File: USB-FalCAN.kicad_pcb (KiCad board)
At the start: 4 copper layers, 76.5 x 30.9 mm, 59 parts, among them J1 Conn_01x17_Pin, J10 CAN, J2 NC, J3 Conn_01x17_Pin, J4 USB2.0_16P, J5 Boot, J6 NC, J7 DE9_Receptacle, J8 RS-485/422-TX, J9 RS-422-RX, SW3 BTN, U1 STM32F042C6Tx, U2 SN65HVD230, U3 SP3485EN, U4 SP3485EN, U5 MIC5504-3.3YM5, Y1 8MHz, Y2 32768Hz

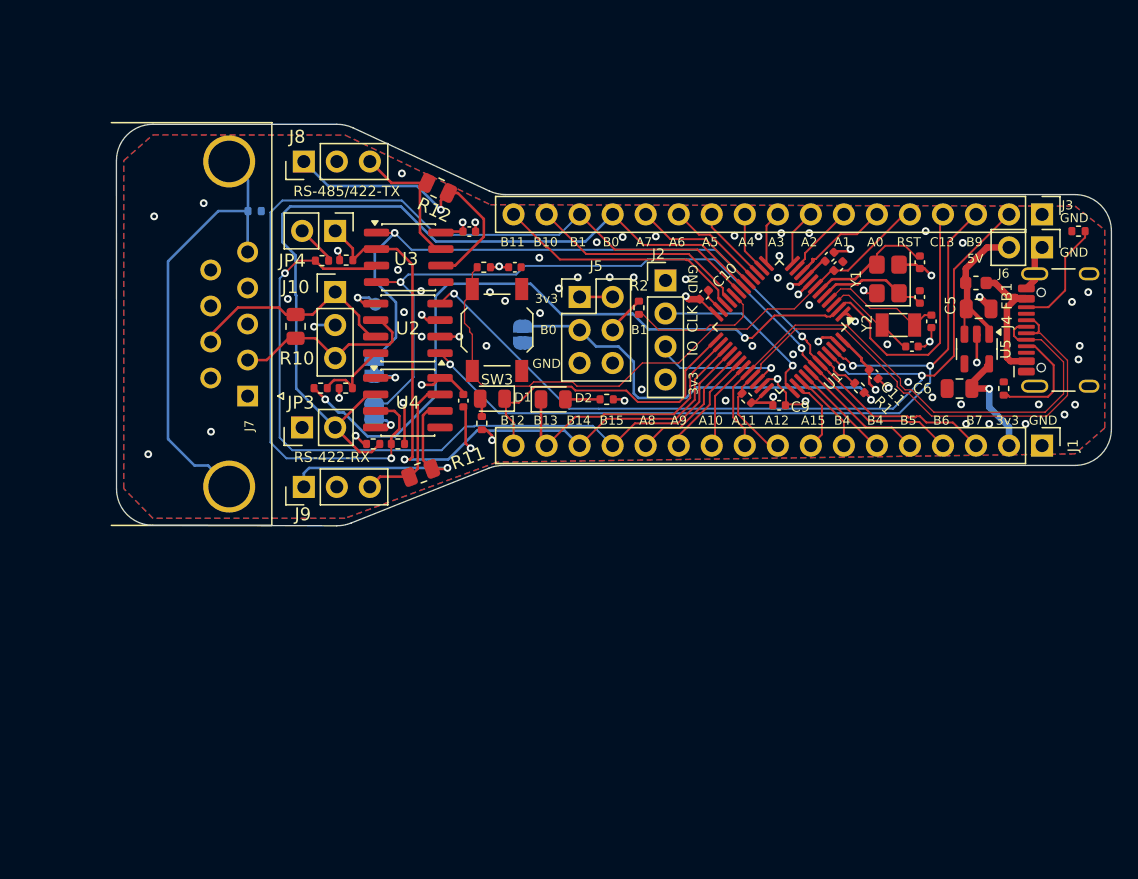
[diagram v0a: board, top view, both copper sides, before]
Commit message: feat: rerouting started
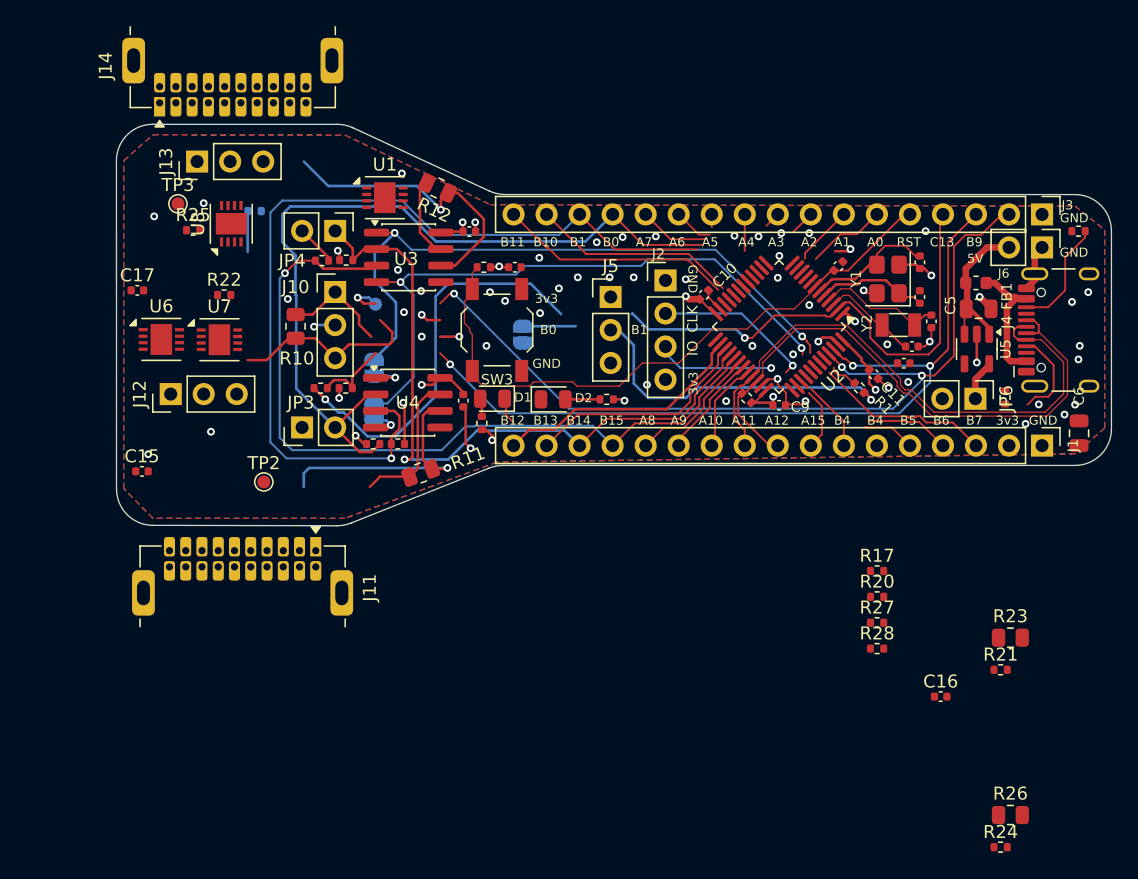
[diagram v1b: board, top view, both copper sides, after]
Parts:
- removed J7: DE9_Receptacle, Connector_Dsub:DSUB-9_Female_Horizontal_P2.77x2.84mm_EdgePinOffset7.70mm_Housed_MountingHolesOffset9.12mm
- removed J8: RS-485/422-TX, Connector_PinHeader_2.54mm:PinHeader_1x03_P2.54mm_Vertical
- removed J9: RS-422-RX, Connector_PinHeader_2.54mm:PinHeader_1x03_P2.54mm_Vertical
- removed R2: 10k, Resistor_SMD:R_0402_1005Metric
- added C15: 100nF, Capacitor_SMD:C_0402_1005Metric, F.Cu at (134.0, 84.5)
- added C16: 100nF, Capacitor_SMD:C_0402_1005Metric, F.Cu at (195.4, 101.8)
- added C17: 100nF, Capacitor_SMD:C_0402_1005Metric, F.Cu at (133.6, 70.6)
- added J11: G125-MH12005L1R, Harwin_Gecko:Harwin_G125-MH12005L1R_2x10_P1.25mm_Horizontal, F.Cu at (147.4, 90.6)
- added J12: CAN, Connector_PinHeader_2.54mm:PinHeader_1x03_P2.54mm_Vertical, F.Cu at (136.2, 78.6)
- added J13: CAN, Connector_PinHeader_2.54mm:PinHeader_1x03_P2.54mm_Vertical, F.Cu at (138.2, 60.7)
- added J14: G125-MH12005L1R, Harwin_Gecko:Harwin_G125-MH12005L1R_2x10_P1.25mm_Horizontal, F.Cu at (135.3, 56.2)
- added JP6: USE_LDO, Connector_PinHeader_2.54mm:PinHeader_1x02_P2.54mm_Vertical, F.Cu at (198.1, 78.9)
- added R17: 10, Resistor_SMD:R_0402_1005Metric, F.Cu at (190.5, 92.2)
- added R20: 10, Resistor_SMD:R_0402_1005Metric, F.Cu at (190.5, 94.2)
- added R21: 5k1, Resistor_SMD:R_0402_1005Metric, F.Cu at (200.0, 99.8)
- added R22: 100k, Resistor_SMD:R_0402_1005Metric, F.Cu at (140.3, 71.0)
- added R23: Rt, Resistor_SMD:R_0805_2012Metric, F.Cu at (200.8, 97.3)
- added R24: 5k1, Resistor_SMD:R_0402_1005Metric, F.Cu at (200.0, 113.4)
- added R25: 100k, Resistor_SMD:R_0402_1005Metric, F.Cu at (137.9, 66.0)
- added R26: Rt, Resistor_SMD:R_0805_2012Metric, F.Cu at (200.8, 111.0)
- added R27: 10, Resistor_SMD:R_0402_1005Metric, F.Cu at (190.5, 96.2)
- added R28: 10k, Resistor_SMD:R_0402_1005Metric, F.Cu at (190.5, 98.2)
- added TP2: VCC/2, TestPoint:TestPoint_Pad_D1.0mm, F.Cu at (143.4, 85.3)
- added TP3: VCC/2, TestPoint:TestPoint_Pad_D1.0mm, F.Cu at (136.8, 64.0)
- added U6: LTC2875-DD, Package_DFN_QFN:DFN-8-1EP_3x3mm_P0.5mm_EP1.66x2.38mm, F.Cu at (135.5, 74.4)
- added U7: LTC2875-DD, Package_DFN_QFN:DFN-8-1EP_3x3mm_P0.5mm_EP1.66x2.38mm, F.Cu at (139.9, 74.4)
- added U8: LTC2875-DD, Package_DFN_QFN:DFN-8-1EP_3x3mm_P0.5mm_EP1.66x2.38mm, F.Cu at (140.9, 65.5)
- C2, C3: value 15pF -> 10pF
- J5: footprint Connector_PinHeader_2.54mm:PinHeader_2x03_P2.54mm_Vertical -> Connector_PinHeader_2.54mm:PinHeader_1x03_P2.54mm_Vertical
- R18: value 100k -> 10k
- U1: value STM32F042C6Tx -> LTC4303IDD; footprint Package_QFP:LQFP-48_7x7mm_P0.5mm -> Package_DFN_QFN:DFN-8-1EP_3x3mm_P0.5mm_EP1.66x2.38mm
- U2: value SN65HVD230 -> STM32G474CETx; footprint Package_SO:SOIC-8_3.9x4.9mm_P1.27mm -> Package_QFP:LQFP-48_7x7mm_P0.5mm
- Y1: value 8MHz -> 16MHz AECQ200
- moved U1 31.9 mm to (152.7, 63.5), turned to 0 degrees
- moved U2 28.5 mm to (183.0, 73.4), turned to -135 degrees
- moved C8 9.98 mm to (192.6, 76.2), turned to 0 degrees
- moved C6 9.82 mm to (206.0, 81.6), turned to 90 degrees
- moved J5 2.39 mm to (170.0, 71.1)
- moved R13 0.69 mm to (200.4, 78.8)
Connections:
- net Net-(J8-Pin_1) renamed /485_TX_H
- net Net-(J8-Pin_3) renamed /485_TX_L
- net Net-(J9-Pin_1) renamed /485_RX_H
- net Net-(J9-Pin_3) renamed /485_RX_L
- C2 pad 1: Net-(U1-PF1) -> Net-(U2-PF1)
- C3 pad 1: Net-(U1-PF0) -> Net-(U2-PF0)
- C4 pad 1: Net-(U1-PC14) -> Net-(U2-PC14)
- C7 pad 1: Net-(U1-PC15) -> Net-(U2-PC15)
- D1 pad 1: /PB12 -> /PA5
- D2 pad 1: /PB13 -> /PA4
- J1 pad 16: /PB13 -> /CAN2_TX
- J1 pad 17: /PB12 -> /CAN2_RX
- J1 pad 6: /PB4 -> /CAN3_TX
- J1 pad 7: /PB3 -> /CAN3_RX
- J10 pad 1: /CAN_H -> /CAN1_H
- J10 pad 3: /CAN_L -> /CAN1_L
- J5 pad 2: +3V3 -> /BOOT0
- J5 pad 3: /BOOT0 -> GND
- R1 pad 2: Net-(U1-PF11) -> /CAN_RX
- R10 pad 1: /CAN_H -> /CAN1_H
- R10 pad 2: /CAN_L -> /CAN1_L
- R15 pad 2: Net-(U2-Rs) -> Net-(U6-RS)
- R16 pad 1: Net-(U2-Rs) -> Net-(U6-RS)
- R18 pad 2: Net-(J7-PAD) -> Net-(U1-RDY)
- TP1 pad 1: Net-(U2-Vref) -> Net-(U6-SPLIT)
- U1 pad 1: +3V3 -> Net-(U1-EN)
- U1 pad 2: /PC13 -> /SCL_OUT
- U1 pad 3: Net-(U1-PC14) -> /I2C1_SCL
- U1 pad 4: Net-(U1-PC15) -> GND
- U1 pad 5: Net-(U1-PF0) -> Net-(U1-RDY)
- U1 pad 6: Net-(U1-PF1) -> /I2C1_SDA
- U1 pad 7: /~{NRST} -> /SDA_OUT
- U1 pad 8: GND -> Net-(U1-VCC)
- U1 pad 9: +3V3 -> GND
- U2 pad 1: /CAN_TX -> +3V3
- U2 pad 2: GND -> /PC13
- U2 pad 3: +3V3 -> Net-(U2-PC14)
- U2 pad 4: /CAN_RX -> Net-(U2-PC15)
- U2 pad 5: Net-(U2-Vref) -> Net-(U2-PF0)
- U2 pad 6: /CAN_L -> Net-(U2-PF1)
- U2 pad 7: /CAN_H -> /~{NRST}
- U2 pad 8: Net-(U2-Rs) -> /PA0
- U5 pad 5: +3V3 -> Net-(JP6-A)
- Y1 pad 1: Net-(U1-PF0) -> Net-(U2-PF0)
- Y1 pad 3: Net-(U1-PF1) -> Net-(U2-PF1)
- Y2 pad 1: Net-(U1-PC15) -> Net-(U2-PC15)
- Y2 pad 2: Net-(U1-PC14) -> Net-(U2-PC14)
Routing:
- net Net-(J7-PAD): track 35.2 -> 0.00 mm
- net /PB12: track 23.1 -> 0.00 mm
- net /PB13: track 20.7 -> 0.00 mm
- net /CAN2_RX: track 0.00 -> 19.6 mm
- net /CAN2_TX: track 0.00 -> 17.6 mm
- net /CAN_H: track 16.0 -> 0.00 mm
- net /CAN_L: track 14.5 -> 0.00 mm
- net /CAN1_L: track 0.00 -> 14.5 mm
- net +3V3: track 42.3 -> 28.7 mm, vias 14 -> 12
- net /PB2: track 10.8 -> 0.00 mm
- net Net-(U2-PF1): track 0.00 -> 9.76 mm
- net Net-(U1-PF1): track 9.76 -> 0.00 mm
- net Net-(U2-PC15): track 0.00 -> 9.58 mm
- net Net-(U1-PC15): track 9.58 -> 0.00 mm
- net /CAN1_H: track 0.00 -> 8.34 mm
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
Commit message: feat: more routing
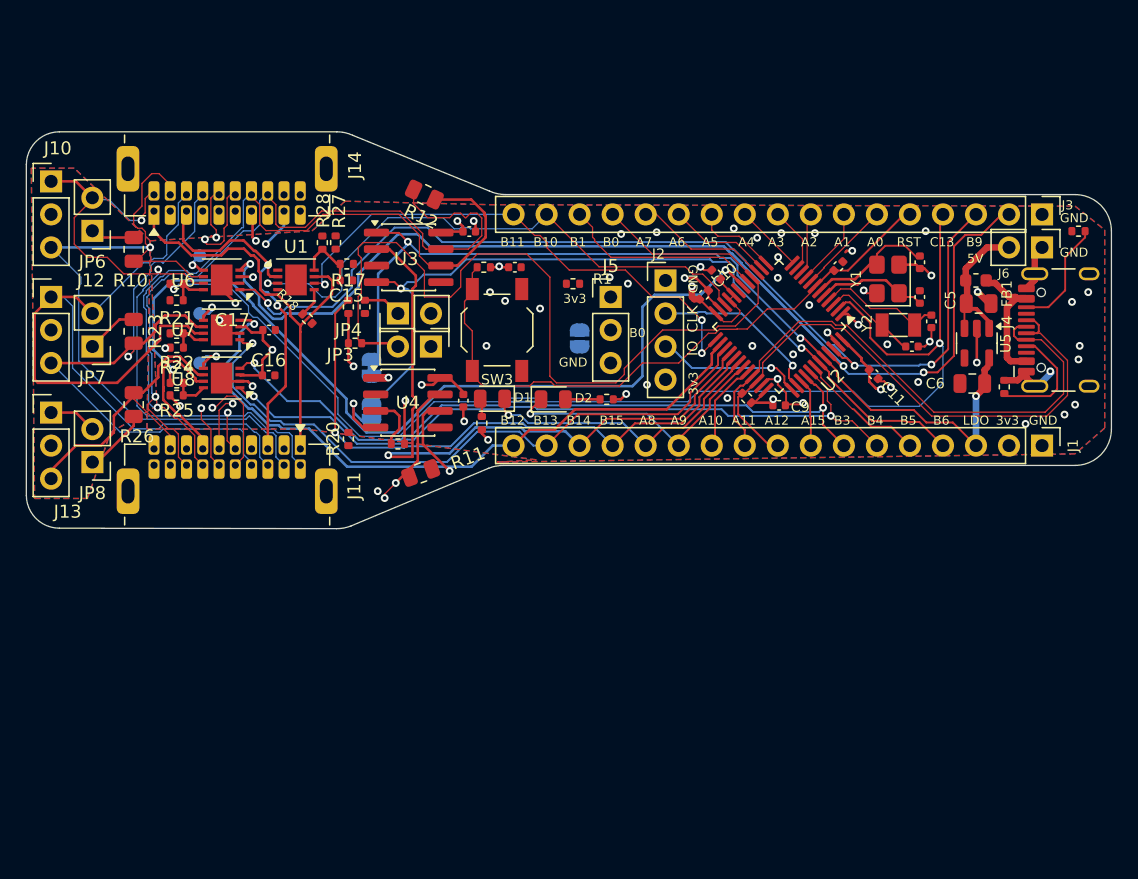
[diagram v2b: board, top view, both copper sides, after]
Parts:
- added JP7: Jumper_2_Open, Connector_PinHeader_2.54mm:PinHeader_1x02_P2.54mm_Vertical, F.Cu at (130.2, 74.9)
- added JP8: Jumper_2_Open, Connector_PinHeader_2.54mm:PinHeader_1x02_P2.54mm_Vertical, F.Cu at (130.2, 83.8)
- JP6: value USE_LDO -> Jumper_2_Open
- R18: moved to F.Cu
- TP2, TP3: moved to B.Cu
- moved R26 74.4 mm to (133.3, 79.4), turned to 90 degrees
- moved R24 72.7 mm to (136.7, 77.7)
- moved R23 71.4 mm to (133.3, 73.8), turned to -90 degrees
- moved JP6 69.1 mm to (130.2, 66.0), turned to 180 degrees
- moved R21 68.4 mm to (136.7, 73.9)
- moved C16 57.3 mm to (143.7, 77.1)
- moved R28 52.9 mm to (147.9, 66.9), turned to 90 degrees
- moved R27 50.9 mm to (148.9, 66.9), turned to -90 degrees
- moved R17 47.1 mm to (149.7, 68.6), turned to 180 degrees
- moved R20 42.4 mm to (149.9, 82.0), turned to 90 degrees
- moved J10 23.4 mm to (127.0, 62.2)
- moved R1 23.4 mm to (167.1, 70.1), turned to 180 degrees
- moved J13 22.3 mm to (127.0, 80.0), turned to 0 degrees
- moved C15 21.5 mm to (149.7, 69.8), turned to 180 degrees
- moved C8 16.0 mm to (178.1, 69.4), turned to 135 degrees
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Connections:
- net /485_RX_H renamed /485_RX_P
- net /485_RX_L renamed /485_RX_N
- net /485_TX_H renamed /485_TX_P
- net /485_TX_L renamed /485_TX_N
- net /CLOCK_H renamed /CLOCK-P
- net /CLOCK_L renamed /CLOCK-N
- C6 pad 1: +3V3 -> /LDO_VOUT
- D1 pad 1: /PA5 -> /PA8
- D2 pad 1: /PA4 -> /PA9
- J1 pad 3: /PB7 -> /LDO_VOUT
- J13 pad 3: /CAN3/CAN_L -> /CAN3_L
- JP6 pad 2: +3V3 -> /CAN1_H
- R10 pad 1: /CAN1_H -> Net-(JP6-A)
- R23 pad 1: /CAN2_H -> Net-(JP7-A)
- R26 pad 1: /CAN3_H -> Net-(JP8-A)
- R26 pad 2: /CAN3/CAN_L -> /CAN3_L
- R27 pad 2: /PA15 -> /PA7
- U5 pad 5: Net-(JP6-A) -> /LDO_VOUT
- U8 pad 6: /CAN3/CAN_L -> /CAN3_L
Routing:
- net /PB2: track 0.00 -> 67.4 mm, vias 0 -> 2
- net /CAN2_H: track 0.00 -> 65.2 mm
- net /CAN3_L: track 0.00 -> 64.3 mm, vias 0 -> 1
- net /CAN3_H: track 0.00 -> 59.6 mm, vias 0 -> 1
- net /CAN3_TX: track 0.00 -> 57.2 mm, vias 0 -> 2
- net /485_TX_N: track 5.83 -> 59.2 mm, vias 0 -> 1
- net /CAN2_L: track 0.00 -> 50.4 mm, vias 0 -> 1
- net /CAN3_RX: track 5.45 -> 55.7 mm, vias 0 -> 2
- net /485_RX_N: track 11.2 -> 61.5 mm, vias 0 -> 2
- net /422_DE: track 69.1 -> 20.0 mm, vias 1 -> 0
- net /CAN1_H: track 8.34 -> 53.5 mm, vias 0 -> 2
- net /485_RX_P: track 19.4 -> 63.9 mm, vias 1 -> 2
- net /CAN1_L: track 14.5 -> 54.4 mm, vias 0 -> 1
- net /485_TX_P: track 22.8 -> 59.3 mm
- net /SDA_OUT: track 0.00 -> 33.3 mm
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- added copper zone on In2.Cu, net GND_C
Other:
- board size 76.5 x 30.9 mm -> 83.4 x 30.5 mm
- board text added: "B3"
- board text added: "LDO"
- board text removed: "B7"
- board text removed: "RS485/422TX"
- board text removed: "RX"
- board text removed: "TX"
- board text removed: "Thank you for buying or making this prototype FalCAN Probe ABNielsen.com/FalCAN"

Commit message: fix: slightly more routing
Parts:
- moved R5 3.85 mm to (149.3, 75.7), turned to 180 degrees
- moved R9 1.07 mm to (149.3, 74.7)
- moved C15 0.25 mm to (149.7, 70.1)
- moved R17 0.25 mm to (149.7, 68.8)
- moved R16 0.20 mm to (136.7, 71.6)
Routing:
- net /PA6: track 8.07 -> 63.8 mm, vias 0 -> 1
- net /PA7: track 10.4 -> 37.0 mm, vias 0 -> 1
- net /485_DE: track 46.6 -> 36.0 mm
- net /422_RE: track 72.8 -> 80.4 mm
- net Net-(U1-EN): track 0.00 -> 5.76 mm
- net +3V3: track 43.1 -> 46.9 mm, vias 14 -> 15
- net /CAN3_L: track 64.3 -> 60.4 mm
- net Net-(JP2-B): track 2.31 -> 0.00 mm, vias 1 -> 0
- net GND: track 45.8 -> 46.9 mm, vias 48 -> 51
- net /SDA_OUT: track 33.3 -> 34.3 mm
- net /CAN_RX: track 82.0 -> 83.0 mm
- net /485_RE: track 54.3 -> 55.3 mm
- net /I2C1_SCL: track 44.2 -> 45.1 mm
- net /CAN_TX: track 77.3 -> 78.1 mm
- net /PPS-N: track 22.3 -> 21.7 mm
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
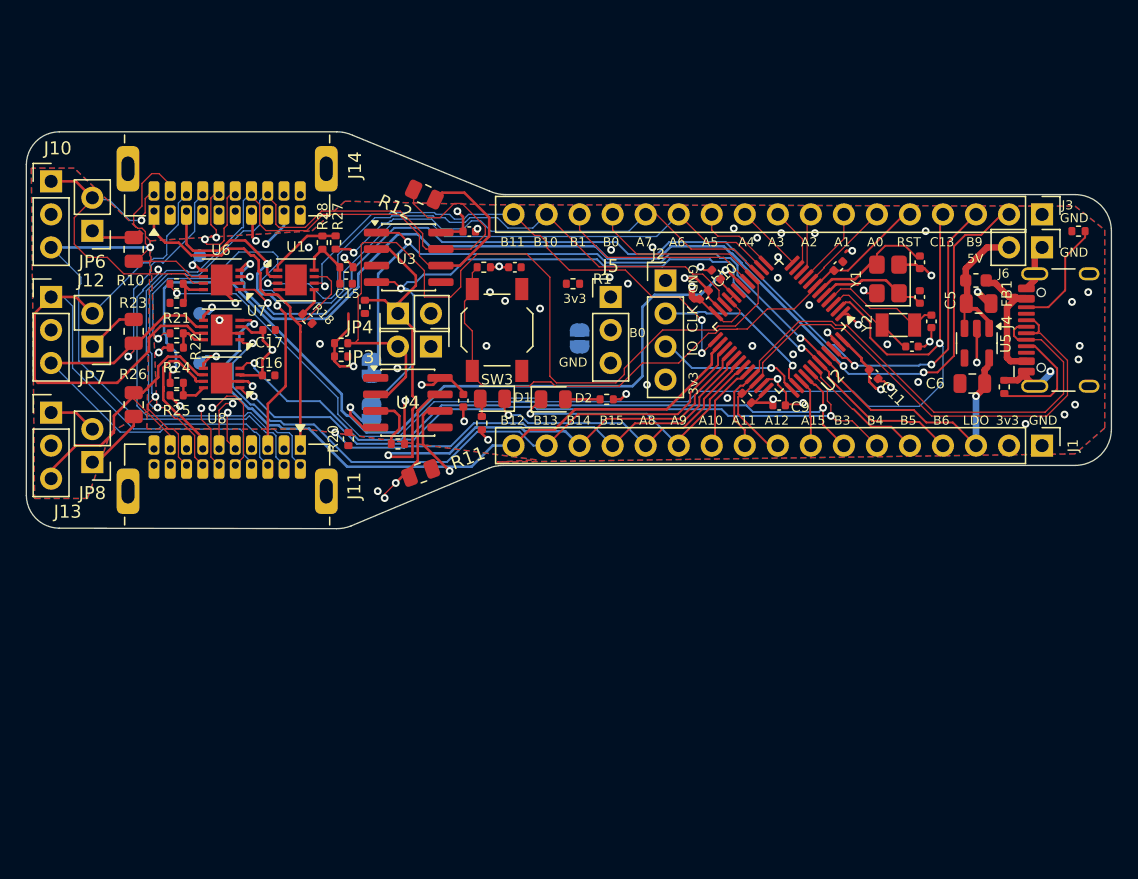
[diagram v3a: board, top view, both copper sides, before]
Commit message: feat: Harwin main connectors
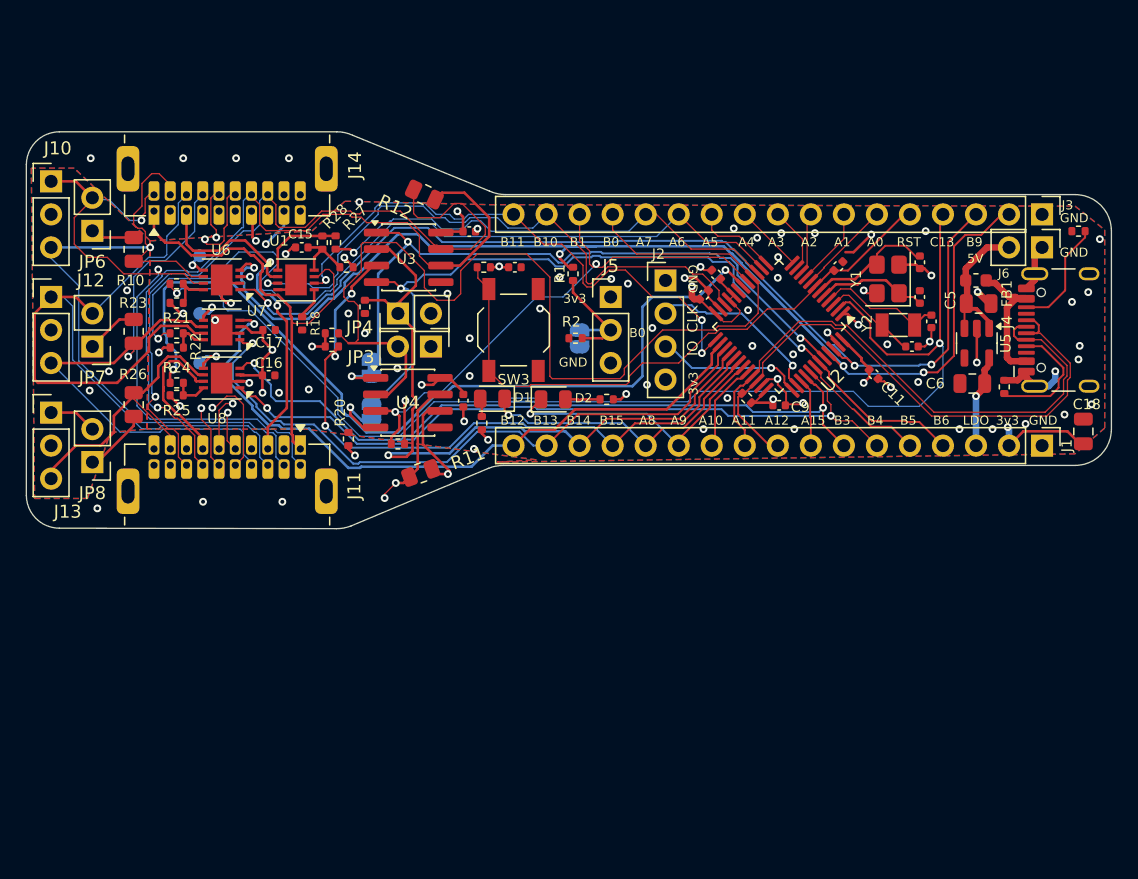
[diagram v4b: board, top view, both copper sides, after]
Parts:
- added C18: 1uF, Capacitor_SMD:C_0805_2012Metric, F.Cu at (206.4, 81.5)
- added R2: 100k, Resistor_SMD:R_0402_1005Metric, F.Cu at (167.3, 74.3)
- moved C15 4.41 mm to (146.3, 67.3), turned to 0 degrees
- moved SW3 1.27 mm to (162.6, 73.7)
- moved R9 1.04 mm to (148.6, 73.9)
- moved R5 1.04 mm to (148.6, 74.9)
- moved R1 0.76 mm to (167.1, 69.3), turned to 90 degrees
- moved R18 0.54 mm to (146.3, 73.2), turned to 90 degrees
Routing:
- net /422_DE: track 20.2 -> 43.9 mm, vias 0 -> 2
- net /485_DE: track 36.0 -> 52.6 mm, vias 1 -> 3
- net /PB7: track 63.9 -> 49.3 mm
- net /BOOT0: track 0.00 -> 9.85 mm
- net +3V3: track 46.9 -> 52.7 mm, vias 15 -> 18
- net /CAN_RX: track 83.0 -> 87.0 mm, vias 3 -> 4
- net /CAN3_H: track 59.6 -> 55.6 mm
- net Net-(JP2-B): track 0.00 -> 3.42 mm, vias 0 -> 1
- net /I2C1_SDA: track 41.6 -> 43.6 mm
- net /485_TX_P: track 59.8 -> 58.2 mm
- net /SDA_OUT: track 34.3 -> 35.9 mm
- net /CAN3_L: track 60.4 -> 59.0 mm
- net /422_RE: track 80.4 -> 81.8 mm
- net /PPS-N: track 21.7 -> 20.4 mm
- net /I2C1_SCL: track 45.1 -> 46.3 mm
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- added copper zone on In3.Cu, net +3V3
- added copper zone on In4.Cu, net GND
- added copper zone on In3.Cu, net GND_C
- removed copper zone on In2.Cu, net +3V3
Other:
- copper layers 4 -> 6
- board text added: "GomSpace FalCAN"
- board text added: "H"
- board text added: "L"
- board text removed: "A"
- board text removed: "ABNielsen.com/FalCAN"
- board text removed: "B"
- board text removed: "CAN-H"
- board text removed: "CAN-L"
- board text removed: "RS-422-RX"
